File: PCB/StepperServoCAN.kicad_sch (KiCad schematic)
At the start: 134 parts, among them J1 CAR, J2 Debug, J3 Motor, J4 Conn_01x06, Q1 AO3401A, Q2 2N7002, Q3 AO3401A, SW1 Rst, U1 STM32F103CBT6, U10 TVS3300DRV, U2 TLE5012B, U3 A4950, U4 A4950, U5 SN65HVD230, U6 LMV321, U7 LMV321, U8 TMAG5170-Q1, U9 ADMT4000BRUZAB-R7, Y1 16Mhz 9pF

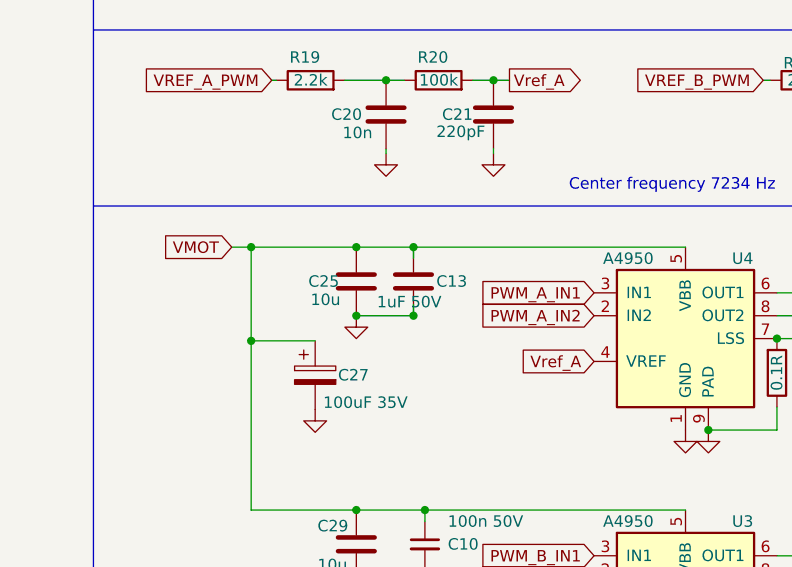
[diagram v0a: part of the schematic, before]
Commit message: pads "excluded form bom"
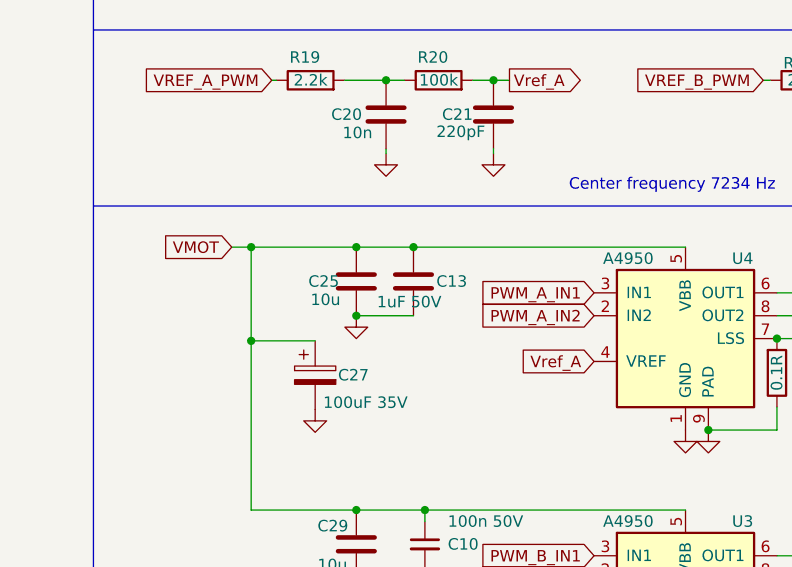
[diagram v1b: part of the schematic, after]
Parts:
- ID1, ID2, JP10, JP11, TP1, TP10, TP12, TP2, TP3, TP4, TP5, TP6, TP7, TP8, TP9: now left out of the parts list
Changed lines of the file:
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@@
 	)
 	(junction
-		(at 50.8 100.33)
-		(diameter 0)
-		(color 0 0 0 0)
-	)
-	(junction
 		(at 191.389 23.876)
 		(diameter 0)
@@
 	)
 	(junction
+		(at 50.8 92.71)
+		(diameter 0)
+		(color 0 0 0 0)
+	)
+	(junction
 		(at 209.804 18.796)
 		(diameter 0)
@@
 	)
 	(junction
-		(at 50.8 92.71)
-		(diameter 0)
-		(color 0 0 0 0)
-	)
-	(junction
 		(at 47.752 74.168)
 		(diameter 0)
@@
 	(wire
 		(pts
-			(xy 44.45 92.71) (xy 50.8 92.71)
-		)
-		(stroke
-			(width 0)
-			(type default)
-		)
-	)
-	(wire
-		(pts
 			(xy 158.75 125.73) (xy 159.385 125.73)
 		)
@@
 	(wire
 		(pts
-			(xy 50.8 92.71) (xy 81.026 92.71)
+			(xy 44.45 92.71) (xy 50.8 92.71)
 		)
 		(stroke
@@
 	(wire
 		(pts
-			(xy 50.8 92.71) (xy 50.8 93.98)
-		)
-		(stroke
-			(width 0)
-			(type default)
-		)
-	)
-	(wire
-		(pts
 			(xy 91.186 132.08) (xy 103.886 132.08)
 		)
@@
 	(wire
 		(pts
+			(xy 44.45 100.33) (xy 50.8 100.33)
+		)
+		(stroke
+			(width 0)
+			(type default)
+		)
+	)
+	(wire
+		(pts
 			(xy 200.914 23.876) (xy 209.804 23.876)
 		)
@@
 	(wire
 		(pts
+			(xy 50.8 92.71) (xy 81.026 92.71)
+		)
+		(stroke
+			(width 0)
+			(type default)
+		)
+	)
+	(wire
+		(pts
 			(xy 32.766 103.124) (xy 32.766 92.71)
 		)
@@
 	(wire
 		(pts
-			(xy 50.8 99.06) (xy 50.8 100.33)
-		)
-		(stroke
-			(width 0)
-			(type default)
-		)
-	)
-	(wire
-		(pts
 			(xy 38.608 25.4) (xy 38.608 24.892)
 		)
@@
 	(wire
 		(pts
-			(xy 50.8 100.33) (xy 44.45 100.33)
-		)
-		(stroke
-			(width 0)
-			(type default)
-		)
-	)
-	(wire
-		(pts
 			(xy 228.6 81.28) (xy 223.52 81.28)
 		)
@@
 		(unit 1)
 		(exclude_from_sim no)
-		(in_bom yes)
+		(in_bom no)
 		(on_board yes)
 		(dnp no)
@@
 		(unit 1)
 		(exclude_from_sim no)
-		(in_bom yes)
+		(in_bom no)
 		(on_board yes)
 		(dnp no)
@@
 		(unit 1)
 		(exclude_from_sim no)
-		(in_bom yes)
+		(in_bom no)
 		(on_board yes)
 		(dnp no)
@@
 		(unit 1)
 		(exclude_from_sim no)
-		(in_bom yes)
+		(in_bom no)
 		(on_board yes)
 		(dnp no)
@@
 		(unit 1)
 		(exclude_from_sim no)
-		(in_bom yes)
+		(in_bom no)
 		(on_board yes)
 		(dnp no)
@@
 		(unit 1)
 		(exclude_from_sim no)
-		(in_bom yes)
+		(in_bom no)
 		(on_board yes)
 		(dnp no)
@@
 		(unit 1)
 		(exclude_from_sim no)
-		(in_bom yes)
+		(in_bom no)
 		(on_board yes)
 		(dnp no)
@@
 		(unit 1)
 		(exclude_from_sim no)
-		(in_bom yes)
+		(in_bom no)
 		(on_board yes)
 		(dnp no)
@@
 		(unit 1)
 		(exclude_from_sim no)
-		(in_bom yes)
+		(in_bom no)
 		(on_board yes)
 		(dnp no)
@@
 		(unit 1)
 		(exclude_from_sim no)
-		(in_bom yes)
+		(in_bom no)
 		(on_board yes)
 		(dnp no)
@@
 		(unit 1)
 		(exclude_from_sim no)
-		(in_bom yes)
+		(in_bom no)
 		(on_board yes)
 		(dnp no)
@@
 		(unit 1)
 		(exclude_from_sim no)
-		(in_bom yes)
+		(in_bom no)
 		(on_board yes)
 		(dnp no)
@@
 		(unit 1)
 		(exclude_from_sim no)
-		(in_bom yes)
+		(in_bom no)
 		(on_board yes)
 		(dnp no)
@@
 		(unit 1)
 		(exclude_from_sim no)
-		(in_bom yes)
+		(in_bom no)
 		(on_board yes)
 		(dnp no)
@@
 		(unit 1)
 		(exclude_from_sim no)
-		(in_bom yes)
+		(in_bom no)
 		(on_board yes)
 		(dnp no)

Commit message: parts availability
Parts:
- D3: footprint Diode_SMD:D_SMA -> Diode_SMD:D_SMB
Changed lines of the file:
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@@
 			)
 		)
-		(property "Footprint" "Diode_SMD:D_SMA"
+		(property "Footprint" "Diode_SMD:D_SMB"
 			(at 31.75 45.085 0)
 			(effects

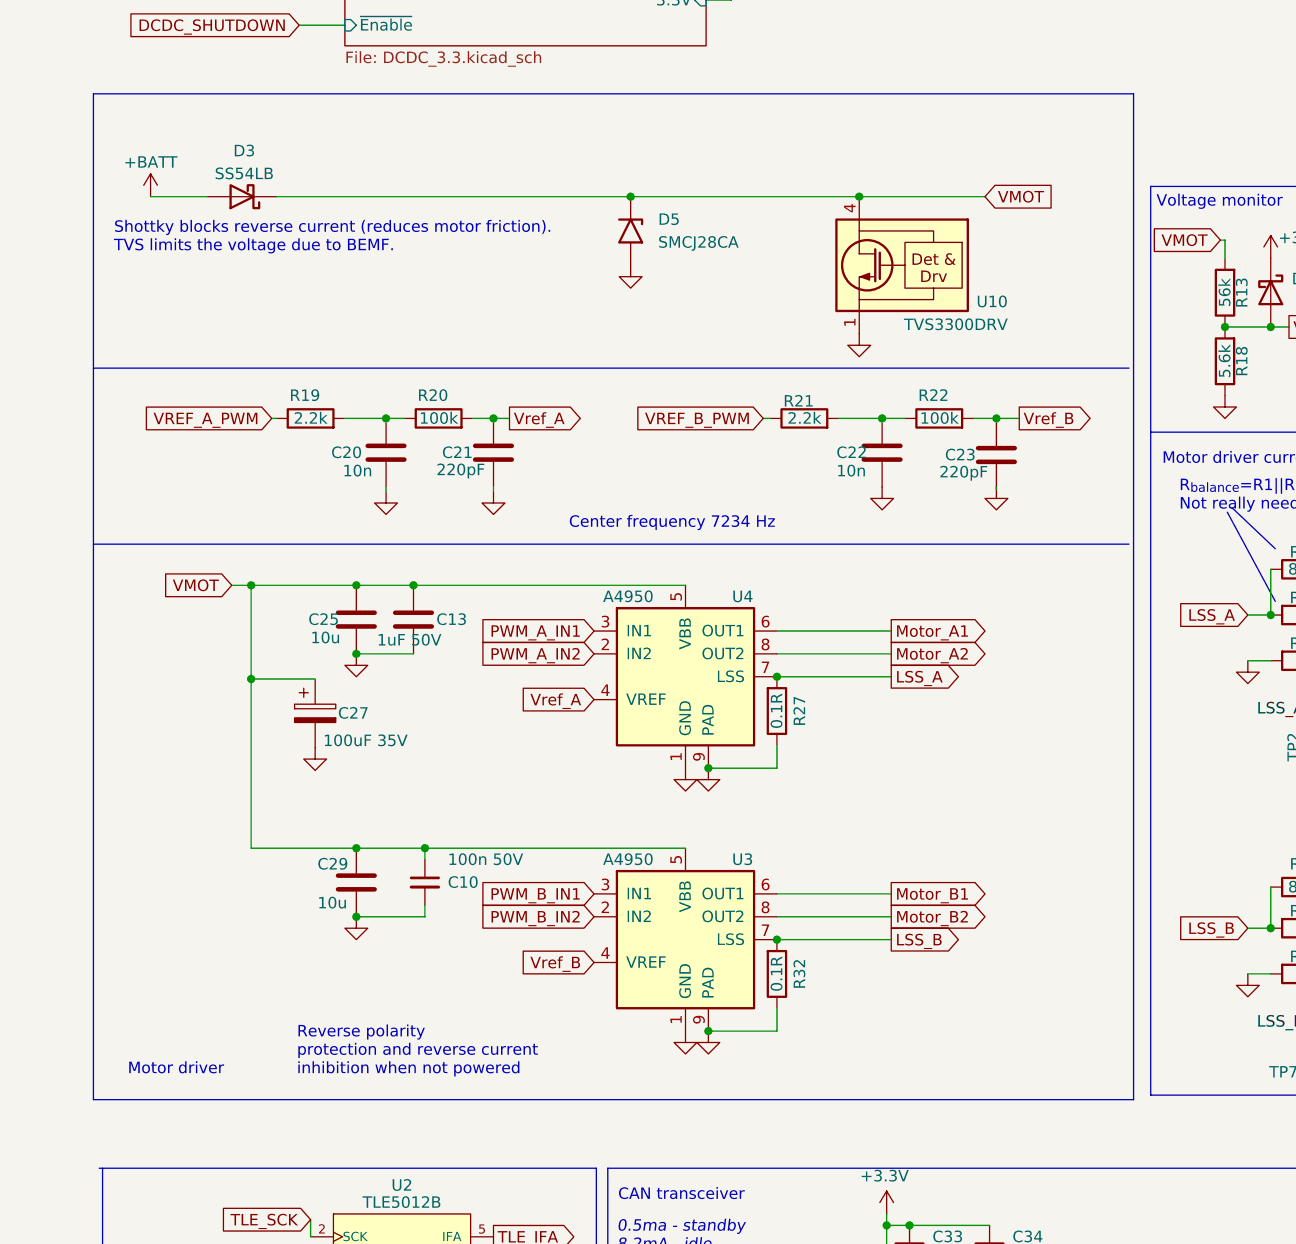
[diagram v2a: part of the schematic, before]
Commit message: Removed one 10uF cap to make more space
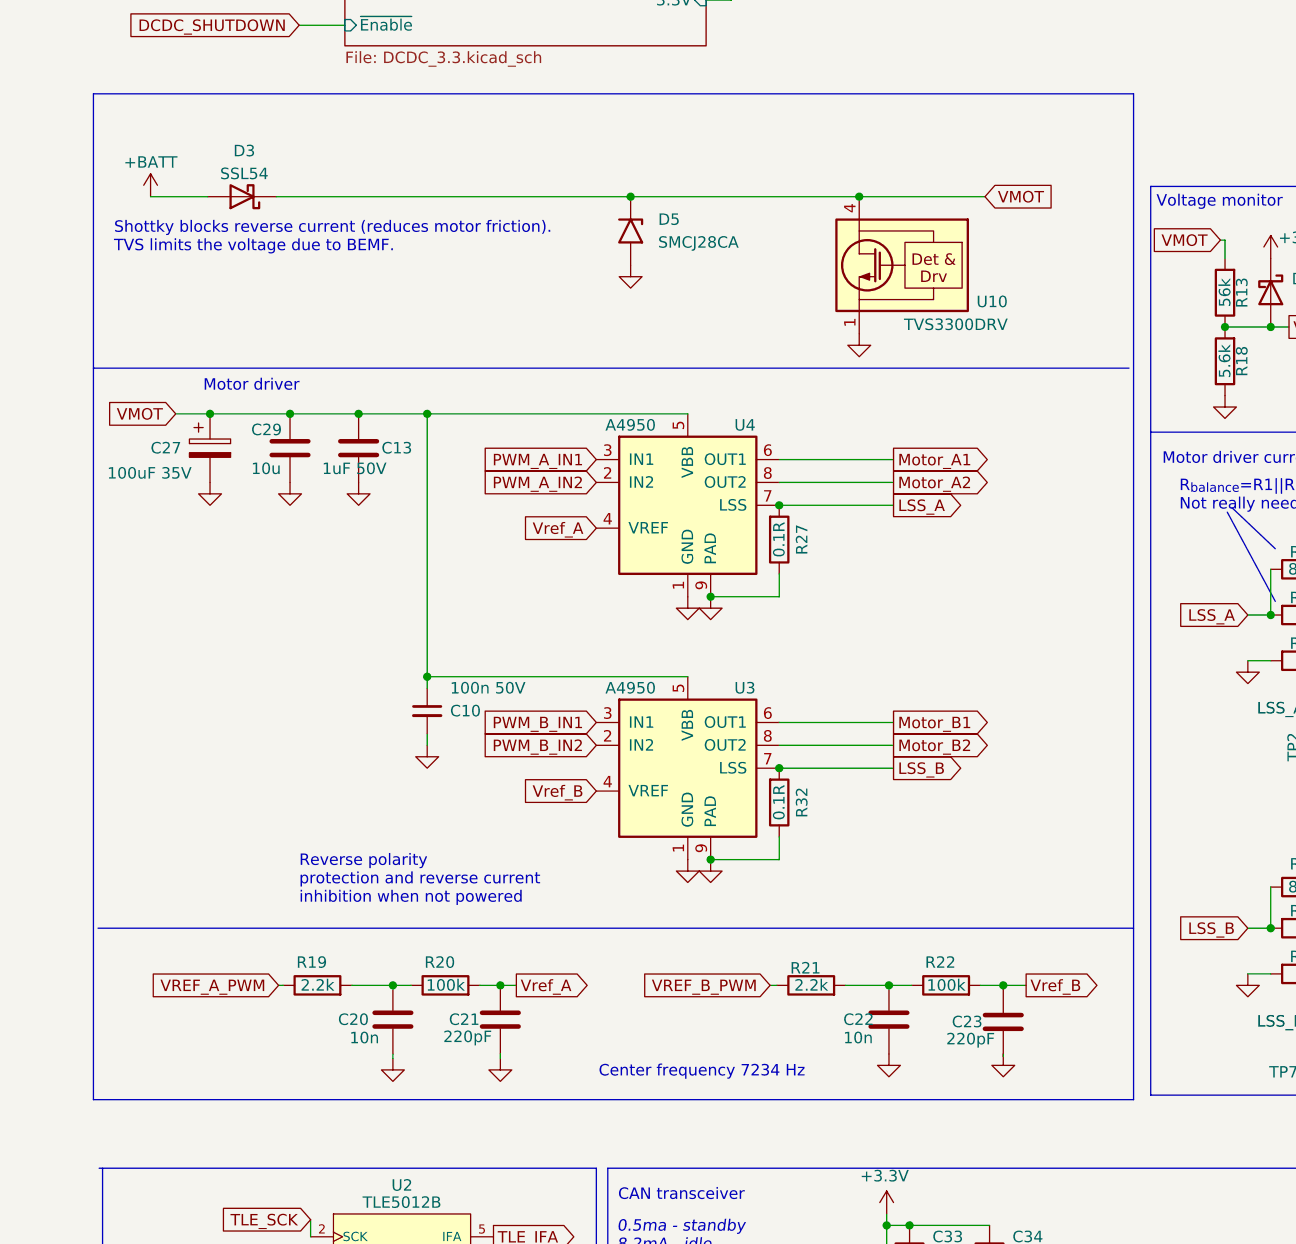
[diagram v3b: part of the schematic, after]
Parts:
- removed C25: 10u, Capacitor_SMD:C_1206_3216Metric, symbol Device:C
- D3: value SS54LB -> SSL54; LCSC C7450527 -> C28646278
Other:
- moved on the sheet: C10, C13, C20, C21, C22, C23, C27, C29, R19, R20, R21, R22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

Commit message: Unidirectional TVS
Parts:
- D5: LCSC C19077606 -> C42371538
- U2: FT Rotation Offset (none) -> 90
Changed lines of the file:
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@@
 			)
 		)
-		(property "LCSC" "C19077606"
+		(property "LCSC" "C42371538"
 			(at 74.93 53.34 0)
 			(effects
@@
 			(effects
 				(font
+					(size 1.27 1.27)
+				)
+				(hide yes)
+			)
+		)
+		(property "FT Rotation Offset" "90"
+			(at 39.37 165.1 0)
+			(effects
+				(font

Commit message: rotations
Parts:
- C27: FT Rotation Offset (none) -> 180
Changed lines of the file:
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@@
+			)
+		)
+		(property "FT Rotation Offset" "180"
+			(at 28.194 77.47 0)
+			(effects
+				(font
+					(size 1.27 1.27)
+				)
+				(hide yes)
 			)
 		)

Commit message: rotations
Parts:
- U2: FT Rotation Offset 90 -> -90
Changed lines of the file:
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@@
 			)
 		)
-		(property "FT Rotation Offset" "90"
+		(property "FT Rotation Offset" "-90"
 			(at 39.37 165.1 0)
 			(effects

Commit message: SOT-23 PESDCAN
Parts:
- D22: LCSC C152727 -> C15771
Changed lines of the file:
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@@
 			)
 		)
-		(property "LCSC" "C152727"
+		(property "LCSC" "C15771"
 			(at 138.43 180.34 90)
 			(effects

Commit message: corrections and todos
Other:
- note added: "todo: remove - less powerfull than TVS"
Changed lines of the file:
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@@
 	(title_block
 		(title "StepperServoCAN")
-		(rev "0.4")
+		(rev "0.5")
 		(company "RetroPilot")
 		(comment 1 "Licensed under CERN-OHL-S v2")
 	)
+	(text "todo:\nremove\n- less powerfull\nthan TVS"
+		(exclude_from_sim no)
+		(at 113.284 55.88 0)
+		(effects
+			(font
+				(size 1.27 1.27)
+				(color 255 0 255 1)
+			)
+			(justify left)
+		)
+	)
 	(text "LSS_ADC = 9.2 x LSS"
